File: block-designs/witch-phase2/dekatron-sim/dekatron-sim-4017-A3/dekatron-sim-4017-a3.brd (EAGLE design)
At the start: 27.9 x 27.9 mm, 21 parts, among them IC1 4017D, IC2 74LVC1G125DBV

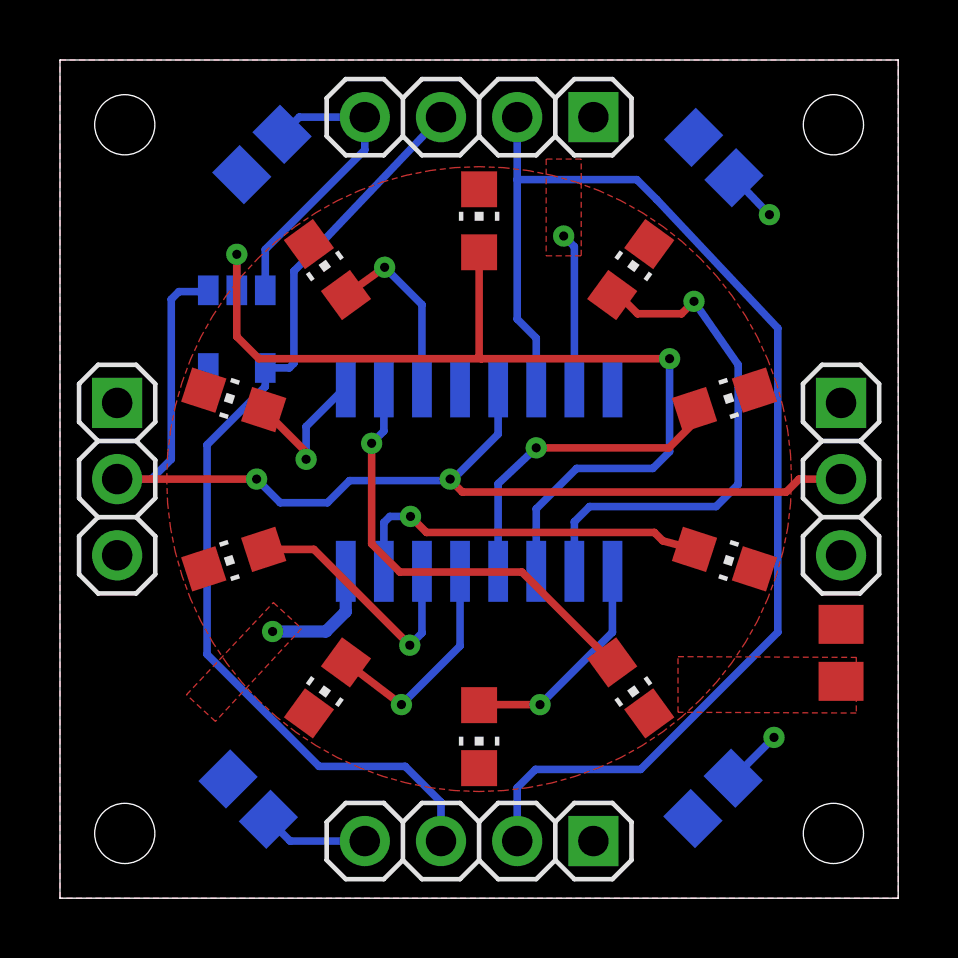
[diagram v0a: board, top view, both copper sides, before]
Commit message: adjust borders for ground/vcc plains and size to match 1.1inch grids
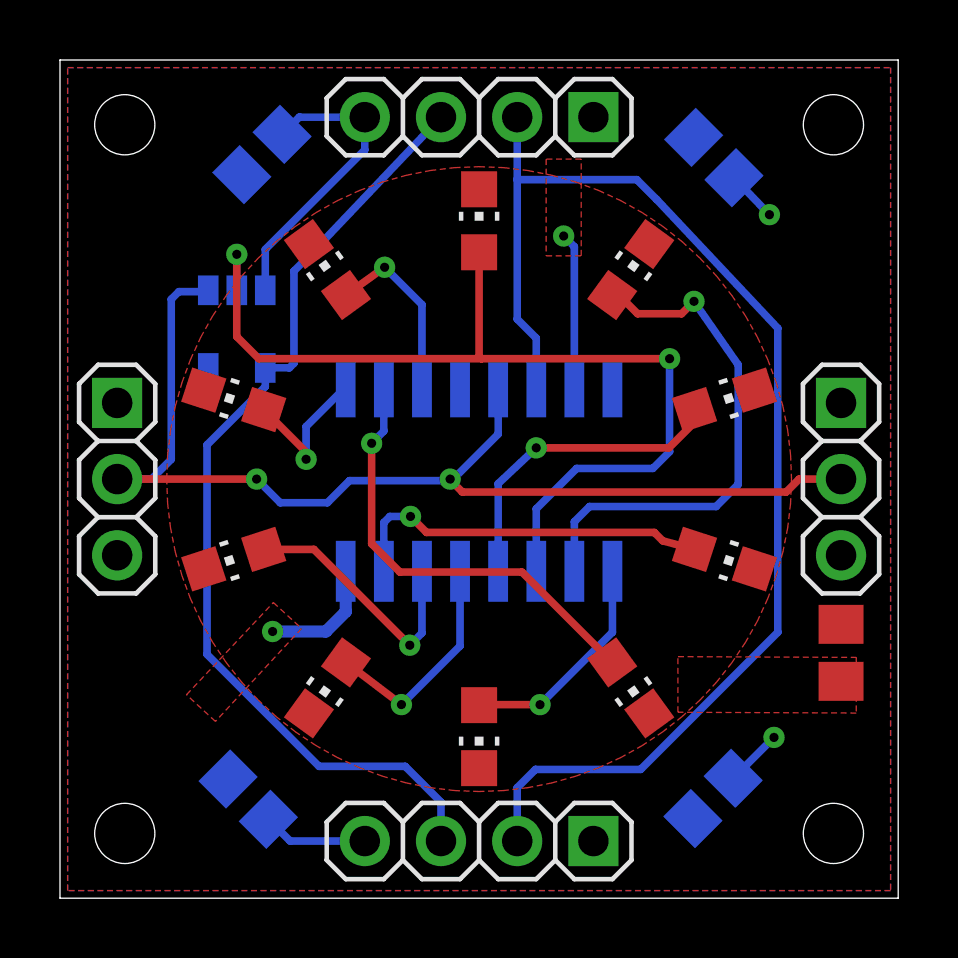
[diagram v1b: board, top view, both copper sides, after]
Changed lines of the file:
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@@
 <contactref element="JP4" pad="4"/>
 <contactref element="IC1" pad="15"/>
-<polygon width="0" layer="1" rank="6">
-<vertex x="27.94" y="0"/>
-<vertex x="0" y="0"/>
-<vertex x="0" y="27.94"/>
-<vertex x="27.94" y="27.94"/>
+<polygon width="0.254" layer="1" rank="6">
+<vertex x="27.686" y="0.254"/>
+<vertex x="0.254" y="0.254"/>
+<vertex x="0.254" y="27.686"/>
+<vertex x="27.686" y="27.686"/>
 </polygon>
 <wire x1="22.439553125" y1="3.99915" x2="23.7998" y2="5.359396875" width="0.254" layer="16"/>
@@
 <contactref element="JP2" pad="1"/>
 <contactref element="JP4" pad="1"/>
-<polygon width="0" layer="16">
-<vertex x="27.94" y="0"/>
-<vertex x="0" y="0"/>
-<vertex x="0" y="27.94"/>
-<vertex x="27.94" y="27.94"/>
+<polygon width="0.254" layer="16">
+<vertex x="27.686" y="0.254"/>
+<vertex x="0.254" y="0.254"/>
+<vertex x="0.254" y="27.686"/>
+<vertex x="27.686" y="27.686"/>
 </polygon>
 <contactref element="JP5" pad="1"/>
